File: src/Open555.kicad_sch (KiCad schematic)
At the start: 45 parts, among them J1 Conn_01x05_Pin, Q1 PNP, Q10 NPN, Q11 NPN, Q12 NPN, Q13 PNP, Q14 PNP, Q15 NPN, Q16 NPN, Q17 PNP, Q18 PNP, Q19 NPN, Q2 PNP, Q20 NPN, Q21 NPN, Q22 NPN, Q3 PNP, Q4 PNP, Q5 PNP, Q6 PNP, Q7 PNP, Q8 NPN, Q9 NPN, SW1 SW_Push

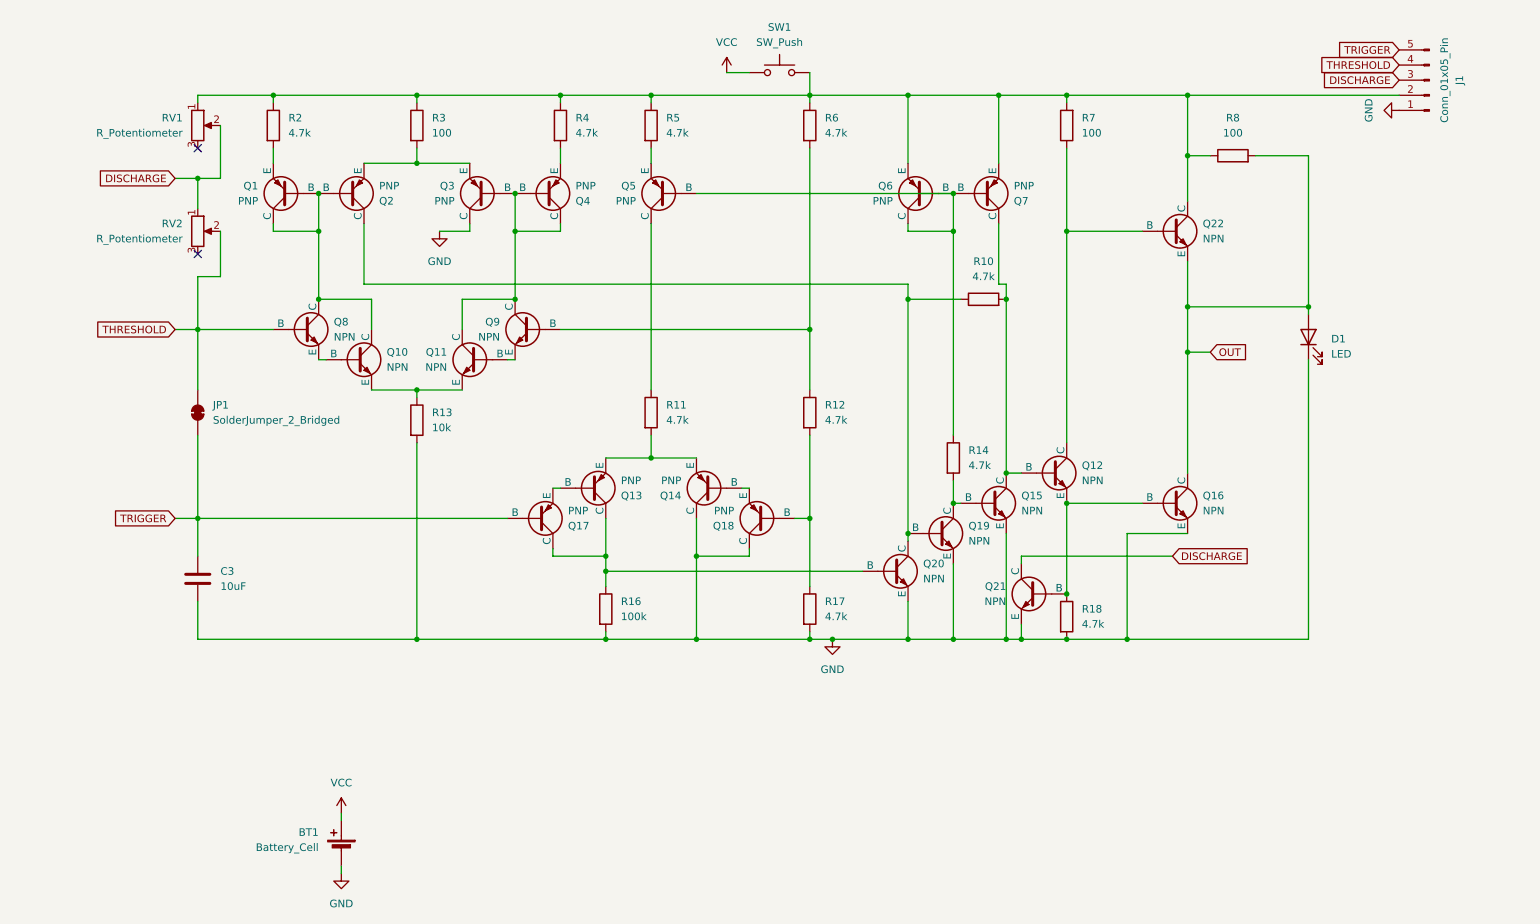
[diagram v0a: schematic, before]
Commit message: Add 3D models
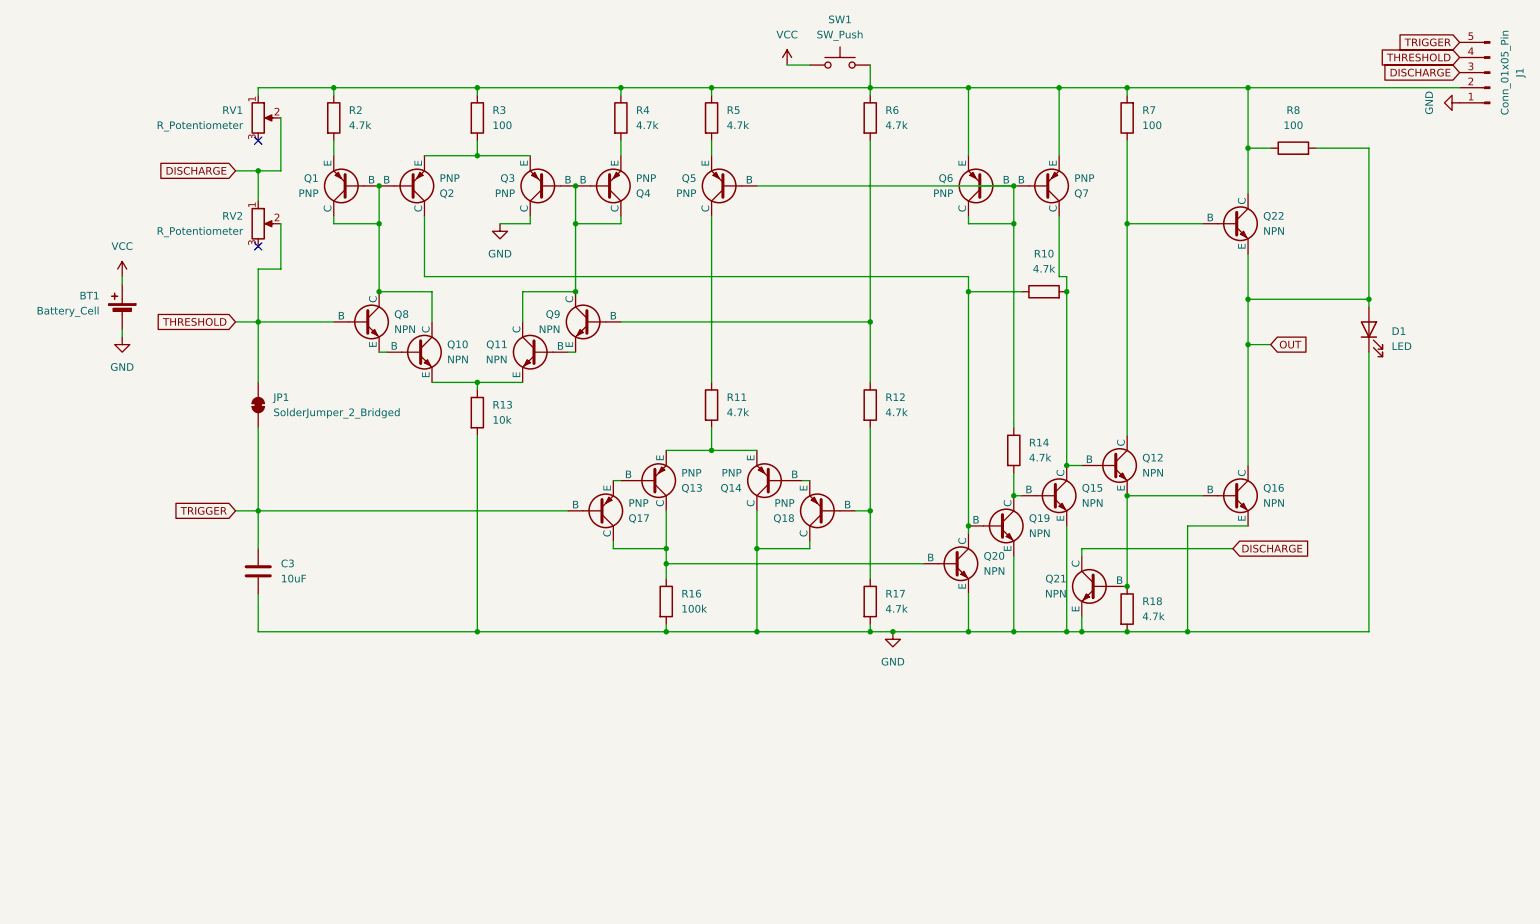
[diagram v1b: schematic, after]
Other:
- moved on the sheet: BT1, C3, D1, J1, JP1, Q1, Q10, Q11, Q12, Q13, Q14, Q15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

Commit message: Final revision
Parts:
- D1: footprint LED_THT:LED_D3.0mm -> LED_THT:LED_D5.0mm
- R3, R7, R8: value 100 -> 220
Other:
- company: (none) -> Hack Club (cheyao)
- title: (none) -> Open555
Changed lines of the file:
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@@
 	(generator_version "9.0")
 	(paper "A4")
+	(title_block
+		(title "Open555")
+		(date "2025-03-26")
+		(rev "V1.2")
+		(company "Hack Club (cheyao)")
+		(comment 1 "Example project for https://github.com/hackclub/solder")
+		(comment 2 "An 555 IC made with hand soldered transistors")
+	)
 	(junction
 		(at 203.2 115.57)
@@
 			)
 		)
-		(property "Value" "100"
+		(property "Value" "220"
 			(at 205.74 38.0999 0)
 			(effects
@@
 			)
 		)
-		(property "Value" "100"
+		(property "Value" "220"
 			(at 96.52 38.0999 0)
 			(effects
@@
 			)
 		)
-		(property "Footprint" "LED_THT:LED_D3.0mm"
+		(property "Footprint" "LED_THT:LED_D5.0mm"
 			(at 243.84 72.39 0)
 			(effects
@@
 			)
 		)
-		(property "Value" "100"
+		(property "Value" "220"
 			(at 231.14 38.1 90)
 			(effects
